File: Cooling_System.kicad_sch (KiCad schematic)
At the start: 12 parts, among them J1 BAT_IN, J2 FAN_OUT, Q1 Q_PMOS_GSD, Q2 Q_NMOS_GDS, U1 Buck_Module

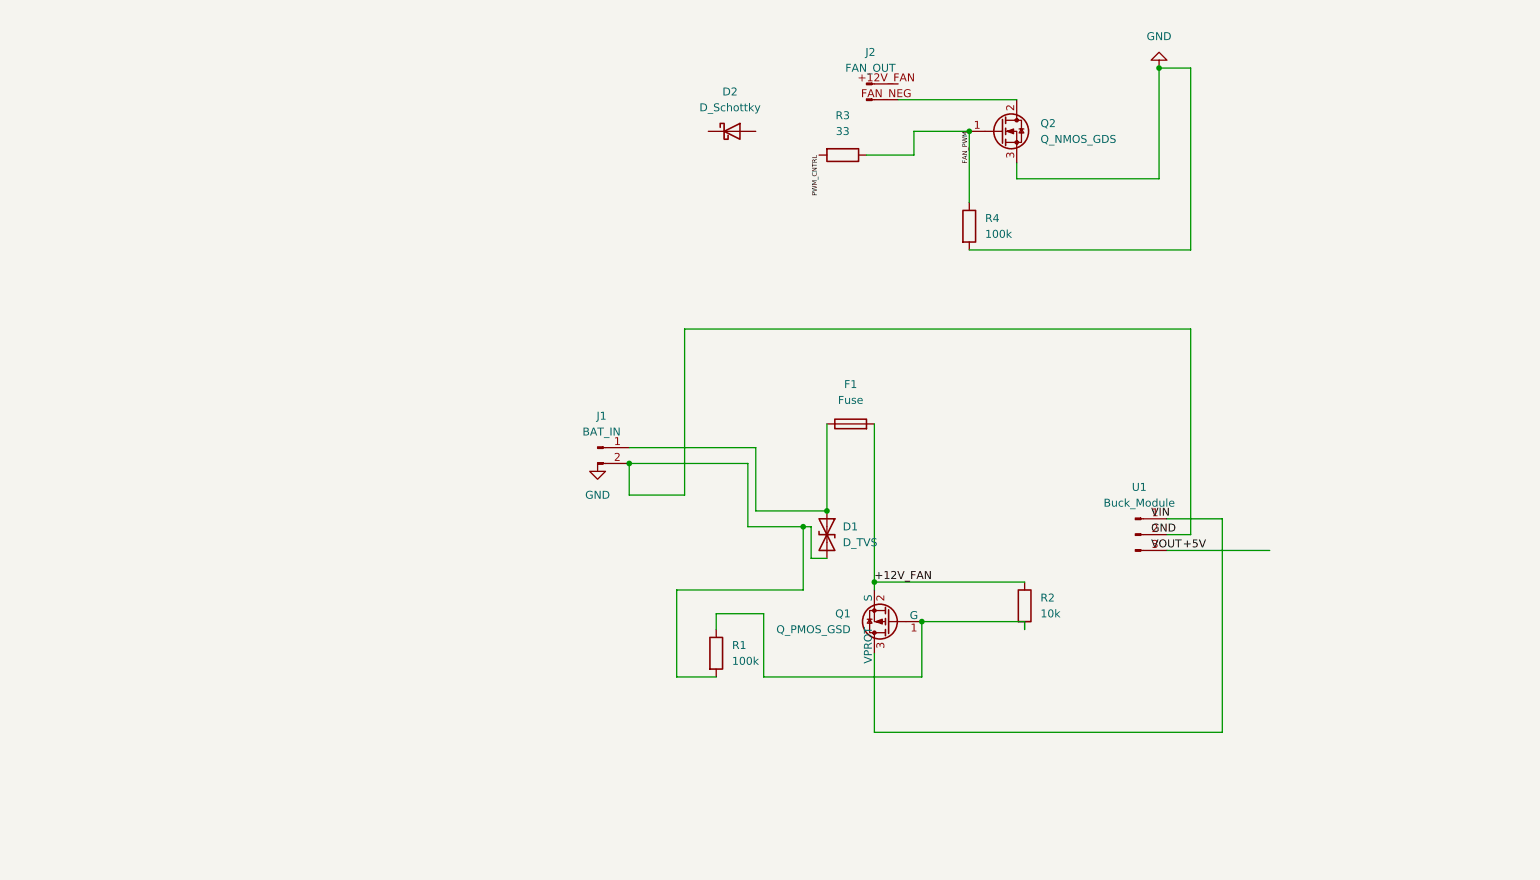
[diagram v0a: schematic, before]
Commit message: circuit schematic with metric logging output
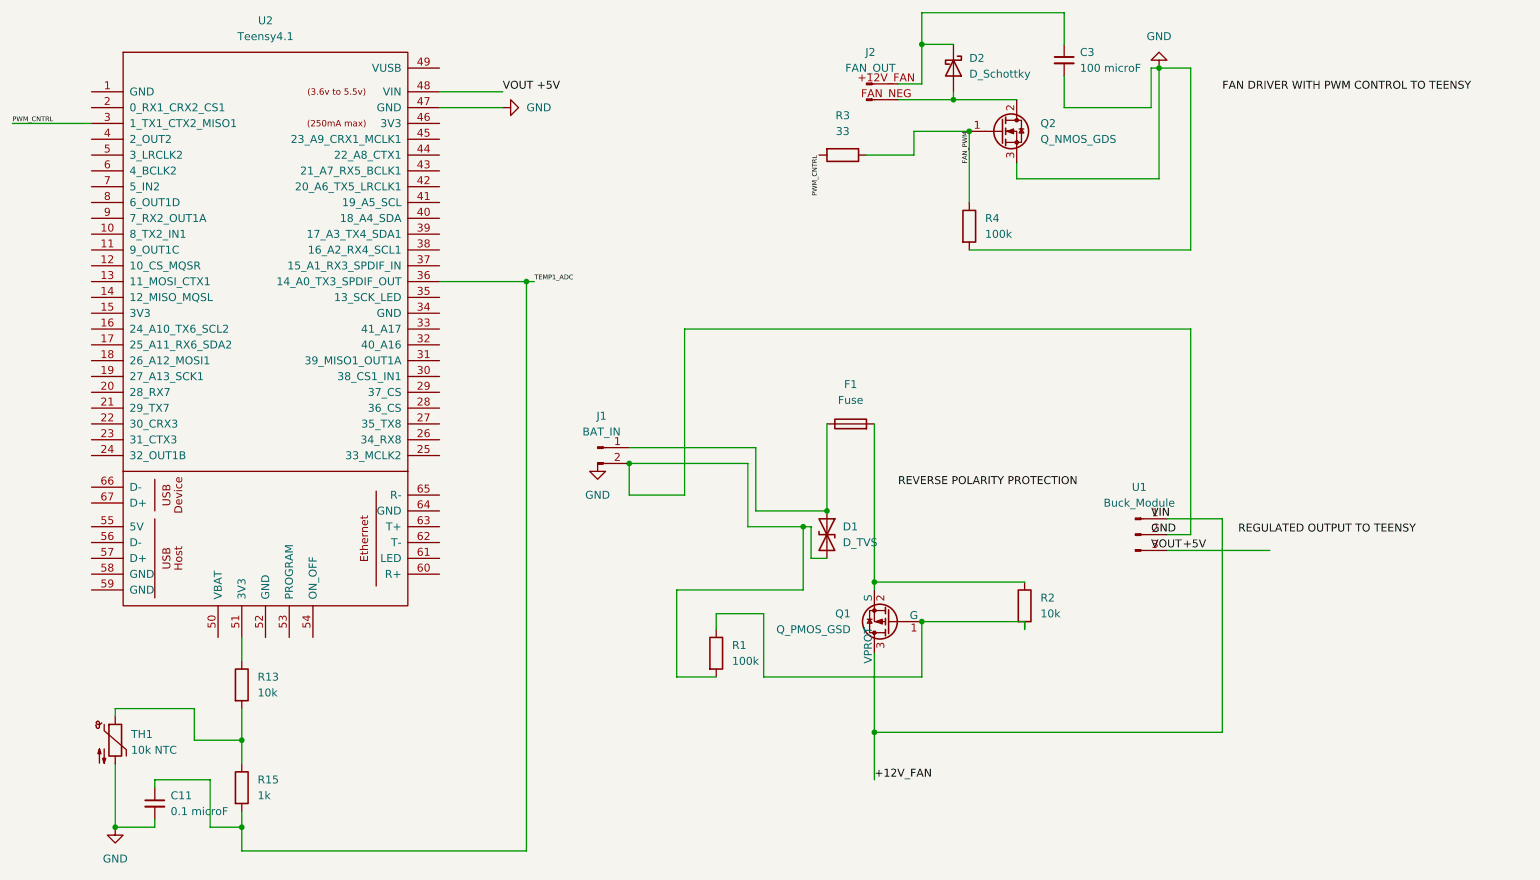
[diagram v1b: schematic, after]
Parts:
- added C11: 0.1 microF, symbol Device:C_Small
- added C3: 100 microF, symbol Device:C_Small
- added R13: 10k, symbol Device:R
- added R15: 1k, symbol Device:R
- added TH1: 10k NTC, symbol Device:Thermistor_NTC
- added U2: Teensy4.1, symbol teensy:Teensy4.1
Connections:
- net +12V_FAN: now also Q1.3 (VPROT), U1.1 (Pin_1); no longer F1.2, Q1.2 (S), R2.1
- net GND: now also C11.2, C3.2, TH1.2, U2.47 (GND)
- net PWM_CNTRL: now also U2.3 (1_TX1_CTX2_MISO1)
- net at D2.1 (K): now also J2.+12V_FAN (Pin_1), C3.1
- net at D2.2 (A): now also J2.FAN_NEG (Pin_2), Q2.2 (D)
- new net: F1.2, Q1.2 (S), R2.1
- new net: R13.2, R15.1, TH1.1
- new net: R13.1, U2.51 (3V3)
- new net TEMP1_ADC: C11.1, R15.2, U2.36 (14_A0_TX3_SPDIF_OUT)
- new net VOUT +5V: U2.48 (VIN)
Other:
- moved on the sheet: D2

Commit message: Cooling System V1
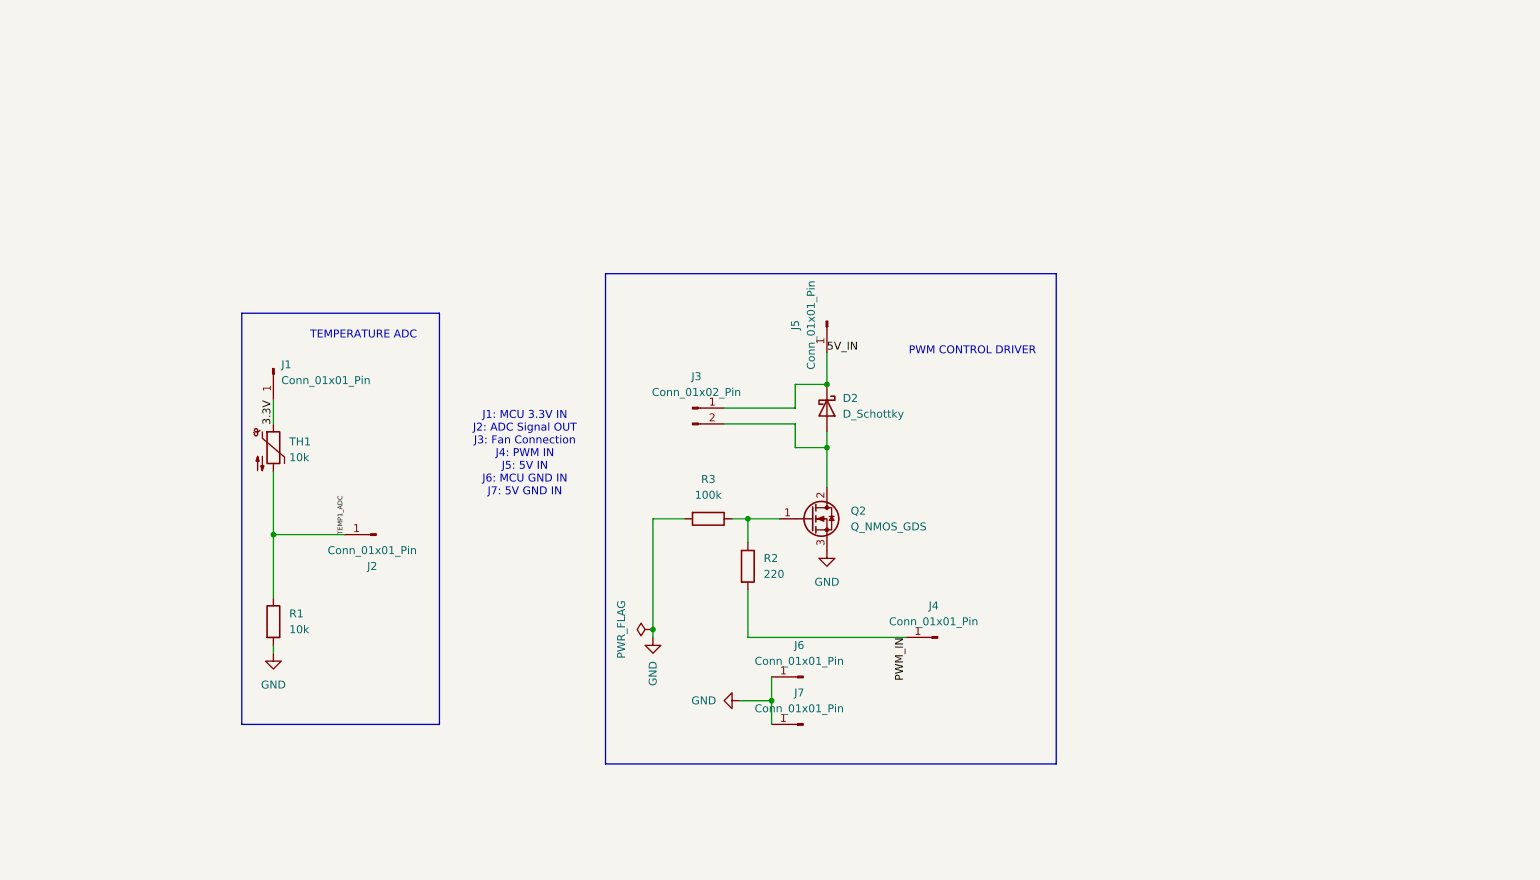
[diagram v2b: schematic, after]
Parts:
- removed C11: 0.1 microF, symbol Device:C_Small
- removed C3: 100 microF, symbol Device:C_Small
- removed D1: D_TVS, symbol Device:D_TVS
- removed F1: Fuse, symbol Device:Fuse
- removed J1: BAT_IN, symbol Connector:Conn_01x02_Pin
- removed J2: FAN_OUT, symbol Connector:Conn_01x02_Pin
- removed Q1: Q_PMOS_GSD, symbol Transistor_FET:Q_PMOS_GSD
- removed R13: 10k, symbol Device:R
- removed R15: 1k, symbol Device:R
- removed R4: 100k, symbol Device:R
- removed U1: Buck_Module, symbol Connector:Conn_01x03_Pin
- removed U2: Teensy4.1, symbol teensy:Teensy4.1
- added J1, J2, J4, J5, J6, J7: Conn_01x01_Pin, Connector_PinHeader_1.00mm:PinHeader_1x01_P1.00mm_Vertical, symbol Connector:Conn_01x01_Pin
- added J3: Conn_01x02_Pin, TerminalBlock:TerminalBlock_MaiXu_MX126-5.0-02P_1x02_P5.00mm, symbol Connector:Conn_01x02_Pin
- D2: footprint (none) -> Diode_THT:D_DO-41_SOD81_P10.16mm_Horizontal
- Q2: footprint (none) -> Package_TO_SOT_THT:TO-220-3_Vertical
- R1: value 100k -> 10k; footprint (none) -> Resistor_THT:R_Axial_DIN0207_L6.3mm_D2.5mm_P7.62mm_Horizontal
- R2: value 10k -> 220; footprint (none) -> Resistor_THT:R_Axial_DIN0207_L6.3mm_D2.5mm_P7.62mm_Horizontal
- R3: value 33 -> 100k; footprint (none) -> Resistor_THT:R_Axial_DIN0207_L6.3mm_D2.5mm_P7.62mm_Horizontal
- TH1: value 10k NTC -> 10k; footprint (none) -> Resistor_THT:R_Axial_DIN0207_L6.3mm_D2.5mm_P2.54mm_Vertical
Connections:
- net FAN_PWM is gone; now on an unnamed net: Q2.1 (G), R3.1
- net PWM_CNTRL is gone; now on net GND: R3.2
- net GND: now also R1.2, J6.1 (Pin_1), J7.1 (Pin_1); no longer TH1.2
- net TEMP1_ADC: now also R1.1, TH1.2, J2.1 (Pin_1)
- net 5V_IN: now reaches D2.1 (K)
- net 5V_IN: now also J3.1 (+FAN_IN), J5.1 (Pin_1)
- net at D2.2 (A), Q2.2 (D): now also J3.2 (-FAN_IN)
- net PWM_IN: now reaches R2.2
- net PWM_IN: now also J4.1 (Pin_1); no longer R1.1
- net 3.3V: now reaches TH1.1
- net 3.3V: now also J1.1 (Pin_1)
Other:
- note added: "J1: MCU 3.3V IN J2: ADC Signal OUT J3: Fan Connection J4: PWM IN J5: 5V IN J6: MCU GND IN J7: 5V GND IN"
- note added: "PWM CONTROL DRIVER"
- note added: "TEMPERATURE ADC"
- moved on the sheet: D2, Q2
